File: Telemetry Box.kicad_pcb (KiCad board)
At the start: 2 copper layers, 103 parts, among them J1 USB_C_Receptacle, J2 DC 5V In, J3 JTAG, J4 Thermistor Molex, J5 Thermistor Molex, J6 Thermistor Molex, J7 Thermistor Molex, Q1 MMBT2222A-TP, SW1 SW_SPDT, SW2 SW_Push, SW3 SW_SPDT, U1 AP2112K-1.8, U2 TPS62160DSG, U3 STM32F373CCTx, U4 LSM6DSRXTR, U5 MCP6L01x-xLT, U6 MCP6L01x-xLT, U7 BMP585, U8 MCP6L01x-xLT, U9 MCP6L01x-xLT, X1 32.768kHz, Y1 8MHz

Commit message: Added MAX-M10S GPS, selected antenna and did schematic
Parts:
- added J8: SMA, Connector_Coaxial:SMA_Amphenol_132289_EdgeMount, F.Cu at (227.1, 90.1)
- added U10: MAX-M10S, RF_GPS:ublox_MAX, F.Cu at (229.2, 102.1)
- R3, R5: value R_US -> 100k
- R4: value R_US -> 312k
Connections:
- C24 pad 1: +3.3V -> +3V3
- C25 pad 1: +3.3V -> +3V3
- C26 pad 1: +3.3V -> +3V3
- C27 pad 1: +3.3V -> +3V3
- C30 pad 1: +3.3V -> +3V3
- C31 pad 1: +3.3V -> +3V3
- R16 pad 2: +3.3V -> +3V3
- R17 pad 2: +3.3V -> +3V3
- R18 pad 2: +3.3V -> +3V3
- R20 pad 2: +3.3V -> +3V3
- R28 pad 2: +3.3V -> +3V3
- R29 pad 2: +3.3V -> +3V3
- R30 pad 2: +3.3V -> +3V3
- R32 pad 2: +3.3V -> +3V3
- U3 pad 19: unconnected-(U3-PB1-Pad19) -> /MCU/GPS_TP
- U3 pad 30: unconnected-(U3-PA9-Pad30) -> /MCU/GPS_SCL
- U3 pad 31: unconnected-(U3-PA10-Pad31) -> /MCU/GPS_SDA
- U3 pad 41: unconnected-(U3-PB5-Pad41) -> /MCU/GPS_RST
- U5 pad 5: +3.3V -> +3V3
- U6 pad 5: +3.3V -> +3V3
- U7 pad 3: +3.3V -> +3V3
- U7 pad 4: +3.3V -> +3V3
- U7 pad 7: +3.3V -> +3V3
- U7 pad 8: +3.3V -> +3V3
- U8 pad 5: +3.3V -> +3V3
- U9 pad 5: +3.3V -> +3V3

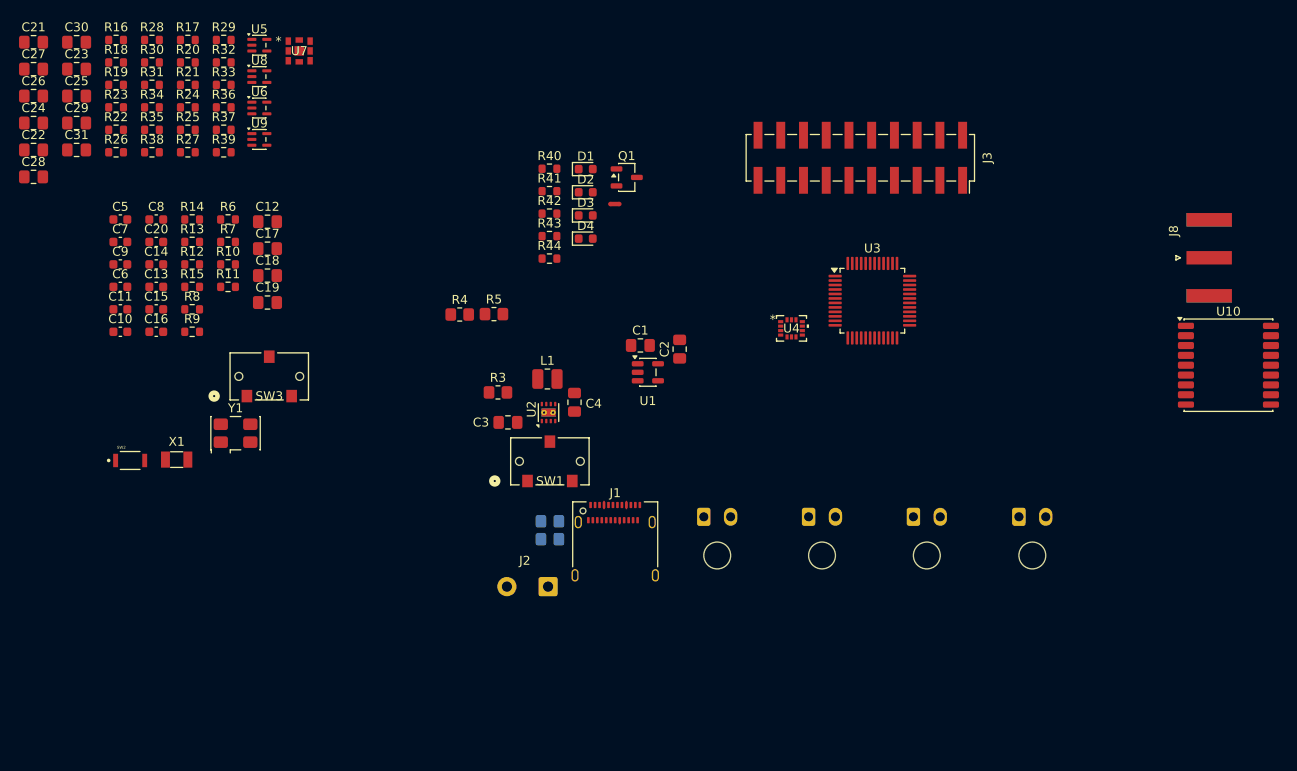
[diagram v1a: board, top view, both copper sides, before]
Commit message: Schematics complete; Starting layout. Removed 2 thermistors, not necessary. Going to update website once layout starts
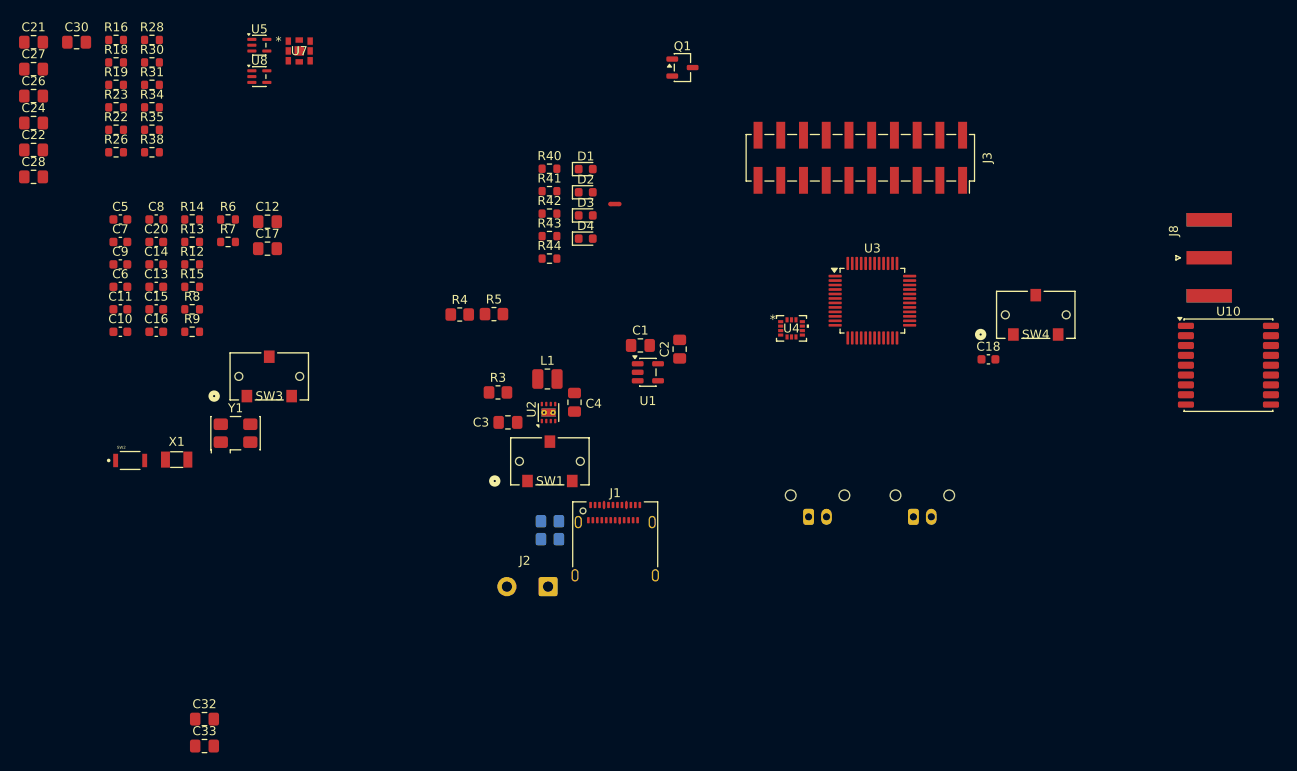
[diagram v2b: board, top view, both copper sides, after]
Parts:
- removed C19, C23, C25, C29, C31: 100nF, Capacitor_SMD:C_0805_2012Metric_Pad1.18x1.45mm_HandSolder
- removed J5, J7: Thermistor Molex, Connector_Molex:Molex_Micro-Fit_3.0_43650-0200_1x02_P3.00mm_Horizontal
- removed R10, R11: 1k, Resistor_SMD:R_0603_1608Metric
- removed R17, R20, R21, R24, R25, R27, R29, R32, R33, R36, R37, R39: 10k, Resistor_SMD:R_0603_1608Metric
- removed U6, U9: MCP6L01x-xLT, Package_TO_SOT_SMD:SOT-353_SC-70-5
- added C32: 100nF, Capacitor_SMD:C_0805_2012Metric_Pad1.18x1.45mm_HandSolder, F.Cu at (114.8, 141.6)
- added C33: 100nF, Capacitor_SMD:C_0805_2012Metric_Pad1.18x1.45mm_HandSolder, F.Cu at (114.8, 144.6)
- added SW4: SW_SPDT, Telem_fp:CL-SB-12B-02T_NDC, F.Cu at (207.7, 96.4)
- C18: footprint Capacitor_SMD:C_0805_2012Metric_Pad1.18x1.45mm_HandSolder -> Capacitor_SMD:C_0603_1608Metric
- J4, J6: footprint Connector_Molex:Molex_Micro-Fit_3.0_43650-0200_1x02_P3.00mm_Horizontal -> Connector_Molex:Molex_MicroClasp_55935-0210_1x02_P2.00mm_Horizontal
- moved C18 81.1 mm to (202.4, 101.4)
- moved Q1 13.8 mm to (168.2, 68.8)
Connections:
- net /MCU/TCK renamed /MCU/SWCLK
- net /MCU/TMS renamed /MCU/SWDIO
- C18 pad 1: /MCU/THERM3_ADC -> /MCU/LOG_EN
- J3 pad 13: /MCU/TDO -> unconnected-(J3-Pin_13-Pad13)
- J3 pad 3: /MCU/TRST -> unconnected-(J3-Pin_3-Pad3)
- J3 pad 5: /MCU/TDI -> unconnected-(J3-Pin_5-Pad5)
- U10 pad 6: Net-(U10-VCC) -> +3V3
- U10 pad 8: Net-(U10-VCC) -> +3V3
- U3 pad 12: /MCU/THERM3_ADC -> unconnected-(U3-PA2-Pad12)
- U3 pad 13: /MCU/THERM4_ADC -> unconnected-(U3-PA3-Pad13)
- U3 pad 38: /MCU/TDI -> unconnected-(U3-PA15-Pad38)
- U3 pad 39: /MCU/TRST -> unconnected-(U3-PB3-Pad39)
- U3 pad 40: /MCU/TDO -> unconnected-(U3-PB4-Pad40)
- U3 pad 45: unconnected-(U3-PB8-Pad45) -> /MCU/LOG_EN

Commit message: Final schematic and initial layout
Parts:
- removed C18: 100nF, Capacitor_SMD:C_0603_1608Metric
- removed D3: 150060VS75000, LED_SMD:LED_0603_1608Metric
- removed NT1: NetTie_2, NetTie:NetTie-2_SMD_Pad0.5mm
- removed R12, R13, R14: 10k, Resistor_SMD:R_0603_1608Metric
- removed R42: 56, Resistor_SMD:R_0603_1608Metric
- removed SW1, SW4: SW_SPDT, Telem_fp:CL-SB-12B-02T_NDC
- added H1: MountingHole_Pad, MountingHole:MountingHole_3.2mm_M3_DIN965_Pad, F.Cu at (179.0, 106.2)
- added H2: MountingHole_Pad, MountingHole:MountingHole_3.2mm_M3_DIN965_Pad, F.Cu at (139.5, 106.2)
- C1, C12, C17, C2, C21, C26, C27, C32, C33: footprint Capacitor_SMD:C_0805_2012Metric_Pad1.18x1.45mm_HandSolder -> Capacitor_SMD:C_0805_2012Metric; moved to B.Cu
- C13, C14, J8, R16, R18, R19, R22, R23, R26, R28, R30, R31, R34, R35, R38, R6, R7, R8, U1, U10, U4, U5, U7, U8, Y1: moved to B.Cu
- C22, C24, C28, C30: footprint Capacitor_SMD:C_0805_2012Metric_Pad1.18x1.45mm_HandSolder -> Capacitor_SMD:C_0603_1608Metric; moved to B.Cu
- C3, C4: footprint Capacitor_SMD:C_0805_2012Metric_Pad1.18x1.45mm_HandSolder -> Capacitor_SMD:C_0805_2012Metric
- SW3: footprint Telem_fp:CL-SB-12B-02T_NDC -> Telem_fp:SWITCH_1SCQN
- moved C27 86.7 mm to (172.3, 109.5)
- moved C26 80.2 mm to (169.6, 103.2)
- moved R18 78.1 mm to (166.6, 116.1), turned to 90 degrees
- moved U10 68.4 mm to (161.1, 107.4), turned to -90 degrees
- moved R28 67.6 mm to (151.1, 118.6), turned to 90 degrees
- moved C30 67.5 mm to (148.0, 114.0), turned to 180 degrees
- moved C33 65.9 mm to (162.9, 99.5), turned to 90 degrees
- moved C28 65.9 mm to (152.8, 114.0)
- moved C21 65.5 mm to (150.3, 102.2), turned to 90 degrees
- moved J8 64.7 mm to (176.2, 130.1), turned to -90 degrees
- moved C5 64.4 mm to (167.6, 102.3)
- moved C7 64.1 mm to (167.6, 103.8)
- moved R16 64.0 mm to (140.9, 118.7), turned to 90 degrees
- moved R15 63.3 mm to (174.4, 110.1), turned to 90 degrees
- moved R34 63.0 mm to (152.6, 118.6), turned to -90 degrees
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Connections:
- C22 pad 1: /Sensors/THERM1 -> /MCU/THERM1
- C28 pad 1: /Sensors/THERM3 -> /MCU/THERM2
- J1 pad A4: USBC_5V -> +5V
- J1 pad A9: USBC_5V -> +5V
- J1 pad B4: USBC_5V -> +5V
- J1 pad B9: USBC_5V -> +5V
- J2 pad 2: /Converters/DCSUPPLY_5V -> +5V
- J3 pad 11: Net-(J3-Pin_11) -> unconnected-(J3-Pin_11-Pad11)
- J3 pad 17: Net-(J3-Pin_17) -> unconnected-(J3-Pin_17-Pad17)
- J3 pad 19: Net-(J3-Pin_19) -> unconnected-(J3-Pin_19-Pad19)
- J4 pad 1: PGND -> /Sensors/THERM1_V-
- J4 pad 2: /Sensors/THERM1_V- -> PGND
- J6 pad 1: PGND -> /Sensors/THERM2_V-
- J6 pad 2: /Sensors/THERM2_V- -> PGND
- R26 pad 1: /Sensors/THERM1 -> /MCU/THERM1
- R38 pad 1: /Sensors/THERM3 -> /MCU/THERM2
- U10 pad 16: /Sensors/GPS_SDA -> /MCU/GPS_SDA
- U10 pad 17: /Sensors/GPS_SCL -> /MCU/GPS_SCL
- U10 pad 4: /Sensors/GPS_TP -> /MCU/GPS_TP
- U10 pad 9: /Sensors/GPS_RST -> /MCU/GPS_RST
- U5 pad 1: /Sensors/THERM1 -> /MCU/THERM1
- U8 pad 1: /Sensors/THERM3 -> /MCU/THERM2
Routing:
- net USBC_5V: track 1.53 -> 0.00 mm
- net Net-(U3-PC14): track 0.00 -> 0.93 mm
- net Net-(C16-Pad2): track 0.00 -> 0.71 mm
- added copper zone on B.Cu, net PGND
- added copper zone on F.Cu, net PGND
- added copper zone on In1.Cu, net PGND
- added copper zone on In2.Cu, net PGND
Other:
- board outline added: 46.9 x 45.1 mm
- copper layers 2 -> 4
- board text added: "Put that back!"

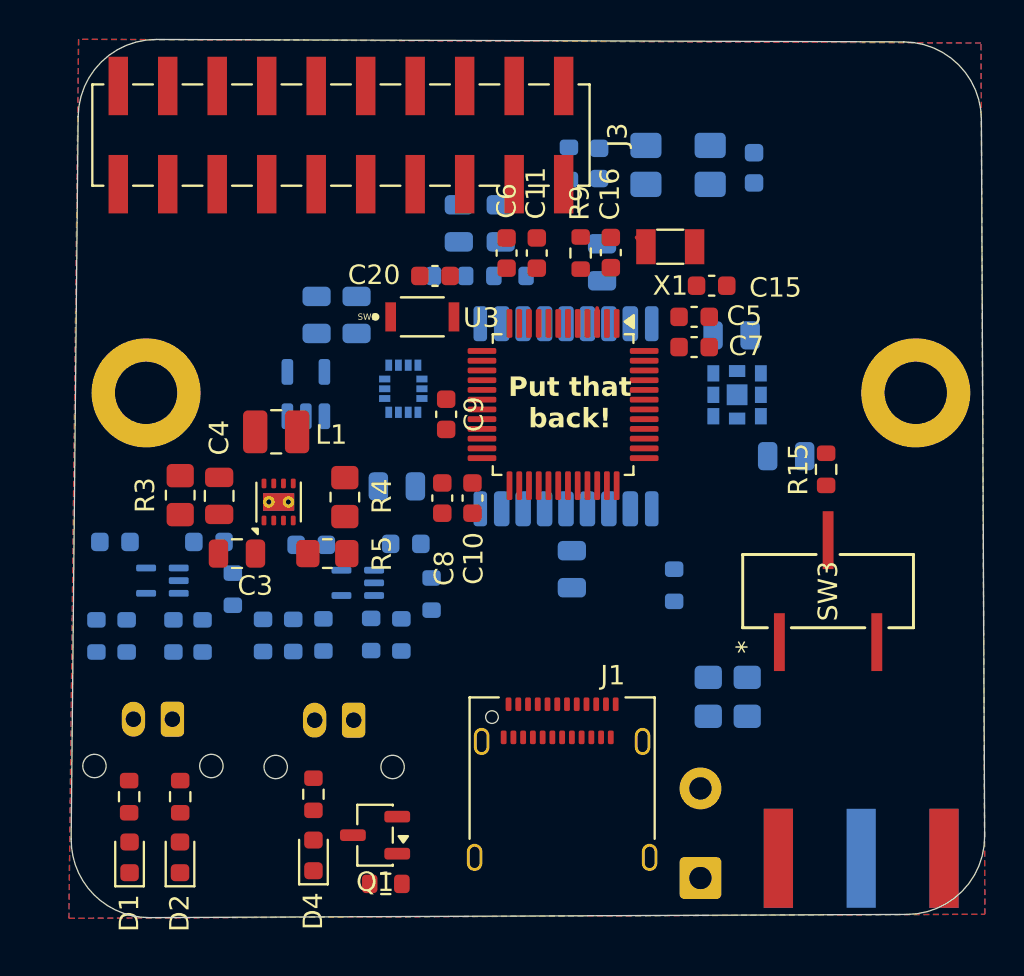
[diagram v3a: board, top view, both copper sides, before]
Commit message: Finished initial signal layout
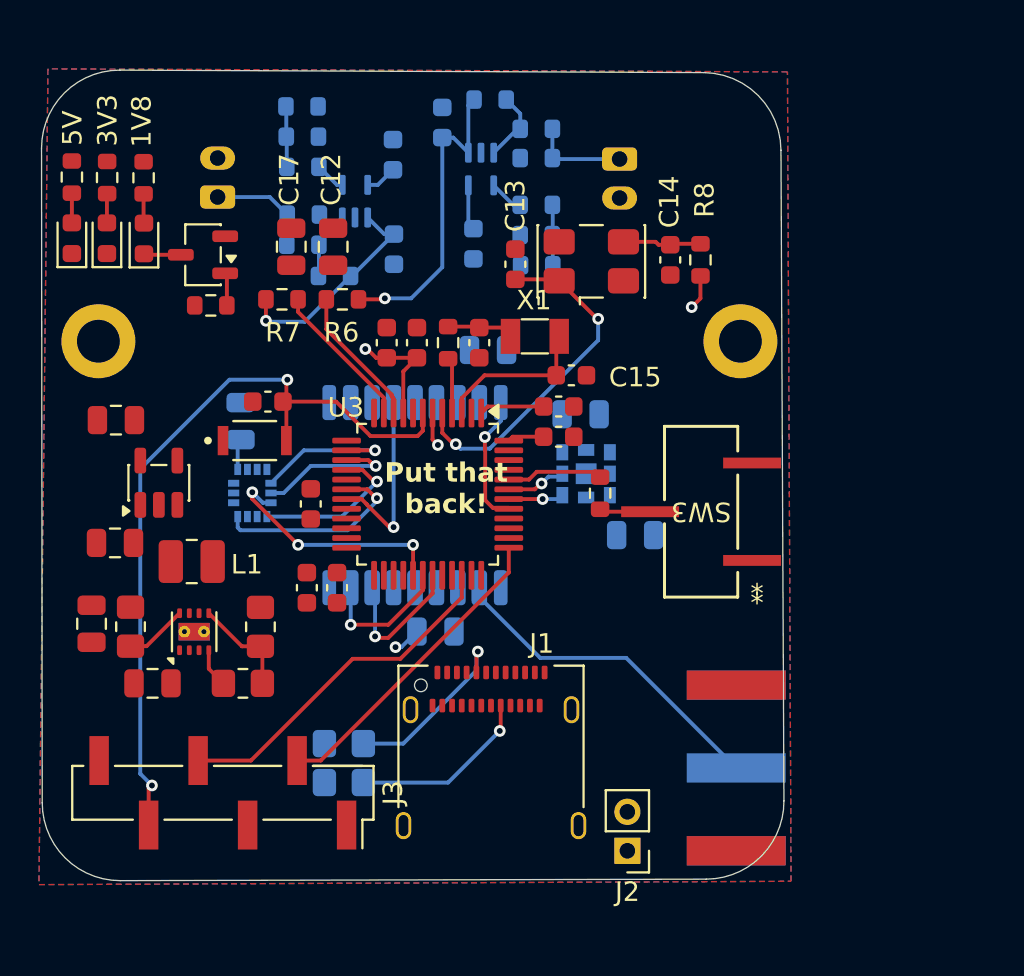
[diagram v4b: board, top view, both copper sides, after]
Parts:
- C1, C12, C13, C14, C17, C2, R6, R7, R8, U1, Y1: moved to F.Cu
- H1, H2: footprint MountingHole:MountingHole_3.2mm_M3_DIN965_Pad -> MountingHole:MountingHole_2.2mm_M2_DIN965_Pad
- J2: footprint Connector_Wire:SolderWire-0.5sqmm_1x02_P4.6mm_D0.9mm_OD2.1mm -> Connector_PinHeader_2.00mm:PinHeader_1x02_P2.00mm_Vertical
- J3: value JTAG -> Conn_01x06; footprint Connector_PinSocket_2.54mm:PinSocket_2x10_P2.54mm_Vertical_SMD -> Connector_PinHeader_2.54mm:PinHeader_1x06_P2.54mm_Vertical_SMD_Pin1Right
- J4, J6: footprint Connector_Molex:Molex_MicroClasp_55935-0210_1x02_P2.00mm_Horizontal -> Connector_Molex:Molex_MicroClasp_55935-0230_1x02_P2.00mm_Horizontal
- moved J4 36.8 mm to (163.8, 94.2), turned to -90 degrees
- moved J3 34.3 mm to (143.4, 126.7)
- moved D4 32.8 mm to (139.4, 98.3)
- moved R44 32.8 mm to (139.4, 95.2)
- moved D2 32.0 mm to (137.5, 98.3)
- moved R41 32.0 mm to (137.5, 95.2)
- moved R40 31.9 mm to (135.7, 95.1)
- moved D1 31.9 mm to (135.7, 98.3)
- moved R22 31.2 mm to (159.5, 92.7), turned to 0 degrees
- moved Q1 31.1 mm to (142.4, 99.1)
- moved R43 31.0 mm to (142.8, 101.7)
- moved R16 30.8 mm to (159.5, 94.2), turned to 180 degrees
- moved R19 30.5 mm to (159.5, 98.1), turned to 0 degrees
- moved R23 30.5 mm to (159.5, 96.5), turned to 0 degrees
- moved R26 28.4 mm to (157.2, 91.2), turned to 0 degrees
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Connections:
- J3 pad 2: +3V3 -> /MCU/SWCLK
- J3 pad 3: unconnected-(J3-Pin_3-Pad3) -> PGND
- J3 pad 4: PGND -> /MCU/SWDIO
- J3 pad 5: unconnected-(J3-Pin_5-Pad5) -> /MCU/RESET
- J3 pad 6: PGND -> unconnected-(J3-Pin_6-Pad6)
- U3 pad 45: /MCU/LOG_EN -> unconnected-(U3-PB8-Pad45)
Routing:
- net /MCU/RESET: track 0.00 -> 40.3 mm, vias 0 -> 2
- net Net-(U3-PF1): track 0.00 -> 20.1 mm, vias 0 -> 2
- net /MCU/SWDIO: track 0.00 -> 18.1 mm
- net Net-(U3-PF0): track 0.00 -> 17.9 mm, vias 0 -> 2
- net Net-(J8-In): track 0.00 -> 17.3 mm
- net +3V3: track 0.00 -> 16.5 mm, vias 0 -> 2
- net /MCU/SWCLK: track 0.00 -> 16.1 mm
- net /MCU/THERM1: track 0.00 -> 16.1 mm, vias 0 -> 1
- net /MCU/IMU_SDI: track 0.00 -> 12.3 mm, vias 0 -> 3
- net /MCU/THERM2: track 0.00 -> 11.3 mm, vias 0 -> 1
- net /MCU/IMU_INT: track 0.00 -> 10.3 mm, vias 0 -> 1
- net Net-(J1-CC1): track 0.00 -> 9.47 mm, vias 0 -> 1
- net Net-(J1-CC2): track 0.00 -> 9.42 mm, vias 0 -> 1
- net /MCU/GPS_TP: track 0.00 -> 9.41 mm, vias 0 -> 1
- net /MCU/IMU_SDO: track 0.00 -> 8.21 mm, vias 0 -> 1
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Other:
- board size 46.9 x 45.1 mm -> 38.1 x 41.6 mm
- board text added: "1V8"
- board text added: "3V3"
- board text added: "5V"

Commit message: Started power routing
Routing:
- net +3V3: track 16.5 -> 23.0 mm, vias 2 -> 5
- net +5V: track 0.00 -> 6.46 mm, vias 0 -> 4
- added copper zone on F.Cu, net +3V3
- added copper zone on F.Cu, net +5V
- added copper zone on F.Cu, net /Converters/5_3V3_SW

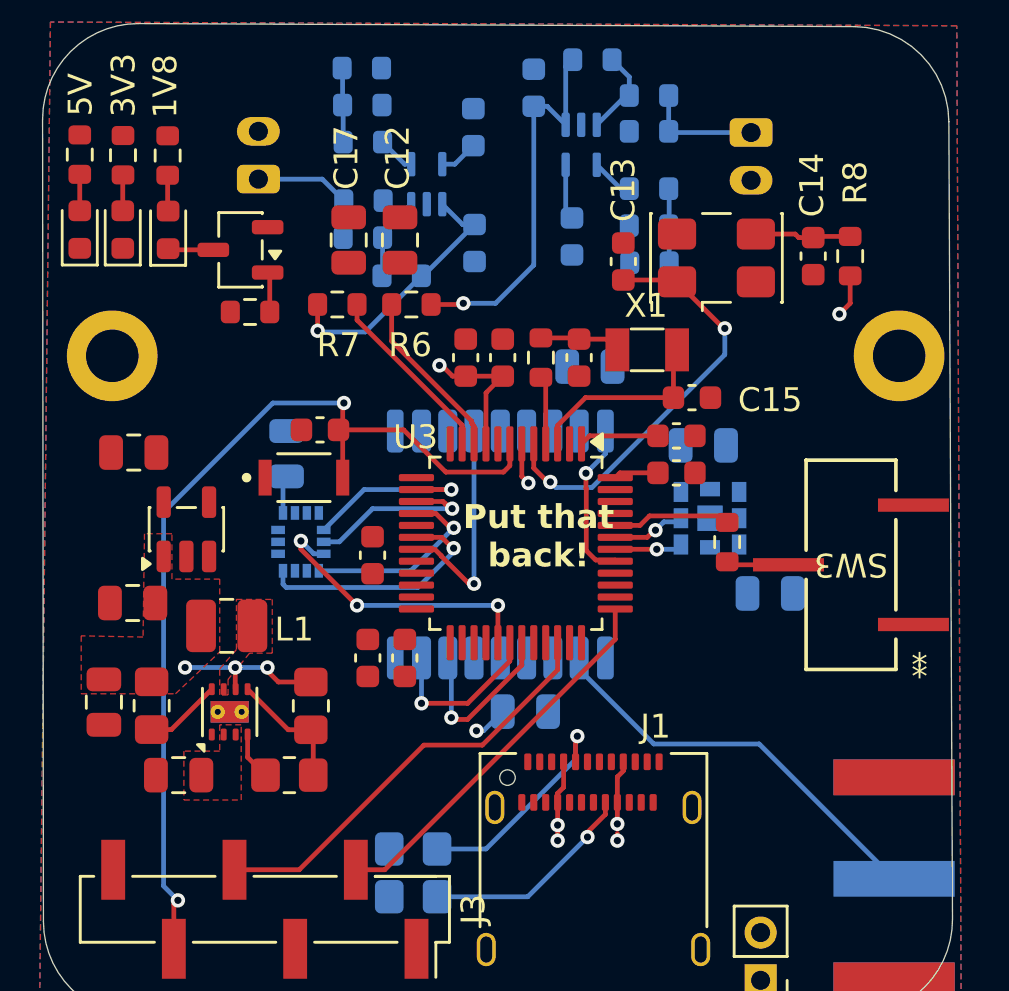
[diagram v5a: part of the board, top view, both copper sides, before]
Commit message: Removed 8Mhz Crystal. Not necessary, not using 72MHz. Also simplifies routing
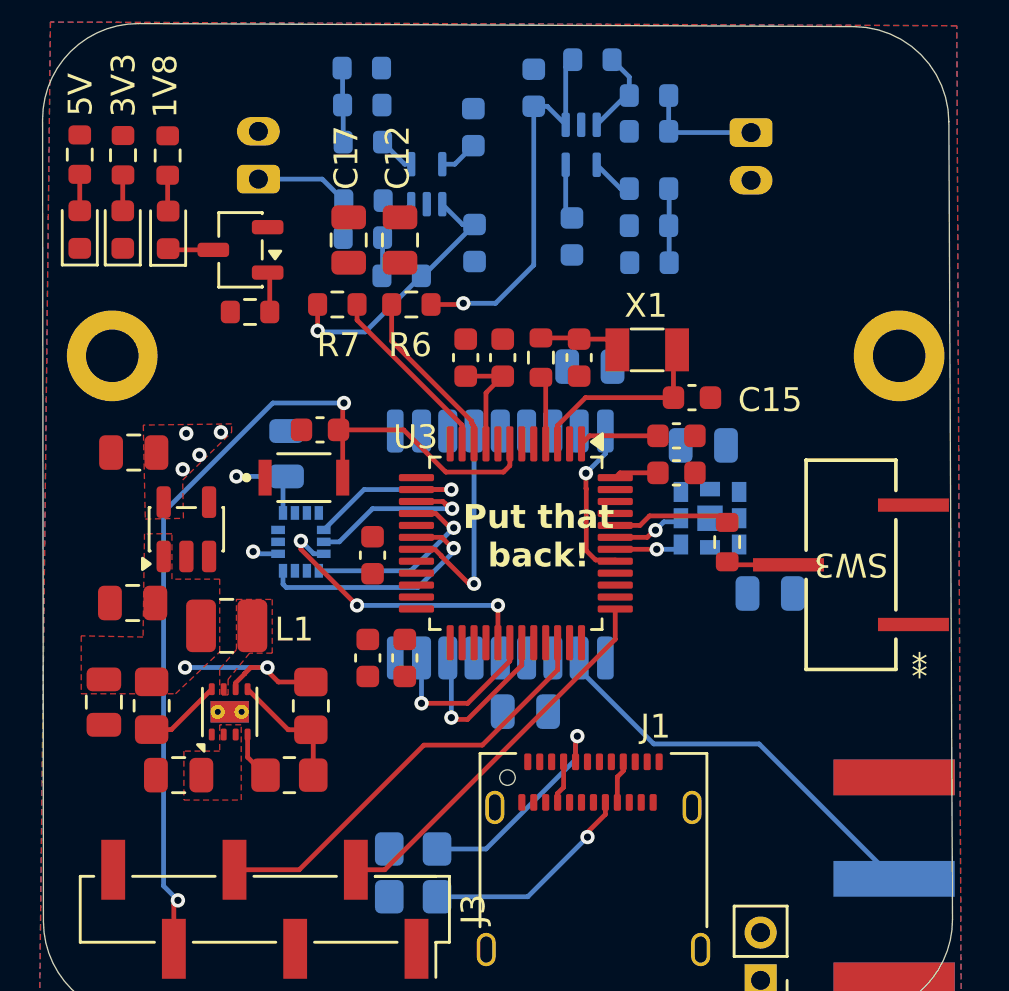
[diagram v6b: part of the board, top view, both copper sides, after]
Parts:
- removed C13, C14: 15pF, Capacitor_SMD:C_0603_1608Metric
- removed R8: 10k, Resistor_SMD:R_0603_1608Metric
- removed Y1: 8MHz, Crystal:Crystal_SMD_5032-4Pin_5.0x3.2mm
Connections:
- U3 pad 5: Net-(U3-PF0) -> unconnected-(U3-PF0-Pad5)
- U3 pad 6: Net-(U3-PF1) -> unconnected-(U3-PF1-Pad6)
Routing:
- net Net-(U3-PF1): track 20.1 -> 0.00 mm, vias 2 -> 0
- net Net-(U3-PF0): track 17.9 -> 0.00 mm, vias 2 -> 0
- net Net-(C14-Pad2): track 4.03 -> 0.00 mm
- net +1V8: track 1.59 -> 4.77 mm, vias 0 -> 6
- net +5V: track 6.46 -> 3.61 mm, vias 4 -> 0
- net +3V3: track 23.0 -> 21.1 mm, vias 5 -> 2
- added copper zone on F.Cu, net +1V8
- added copper zone on In2.Cu, net +1V8
